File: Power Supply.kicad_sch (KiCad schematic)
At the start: 3 parts, among them J2 High Power Supply

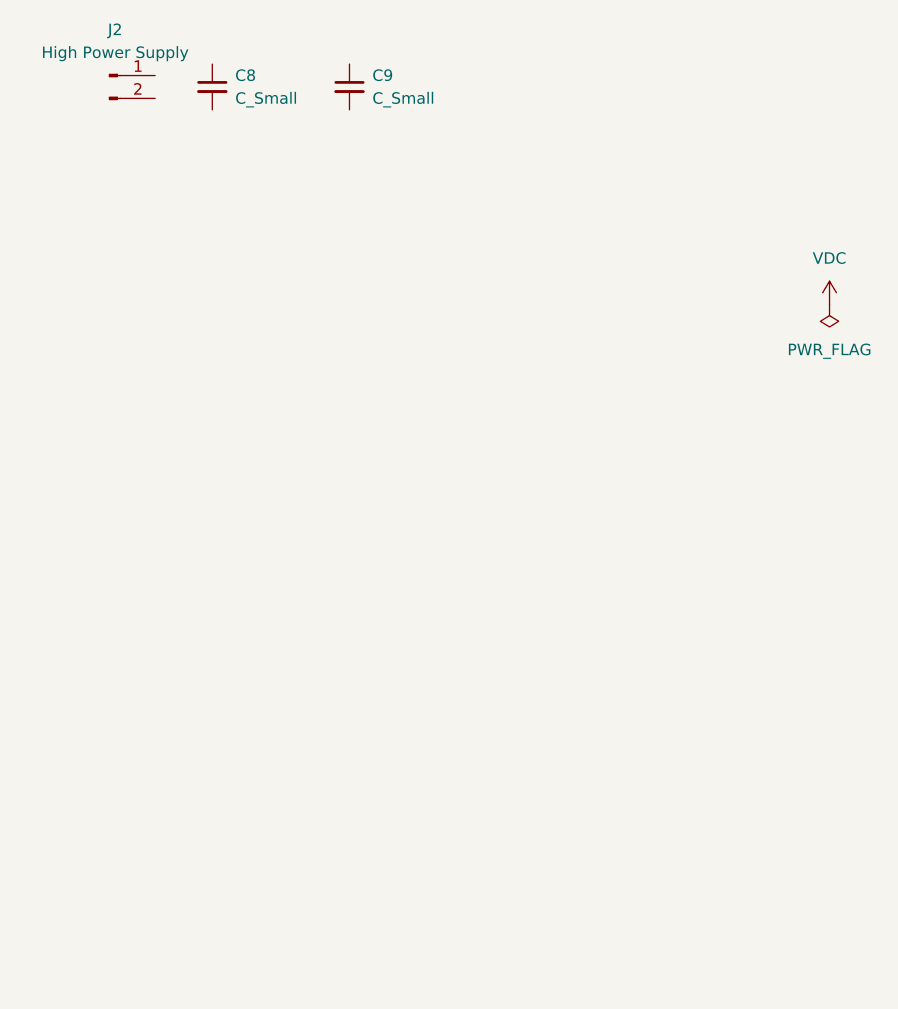
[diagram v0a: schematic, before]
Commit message: Pullup/pulldowns Footprints
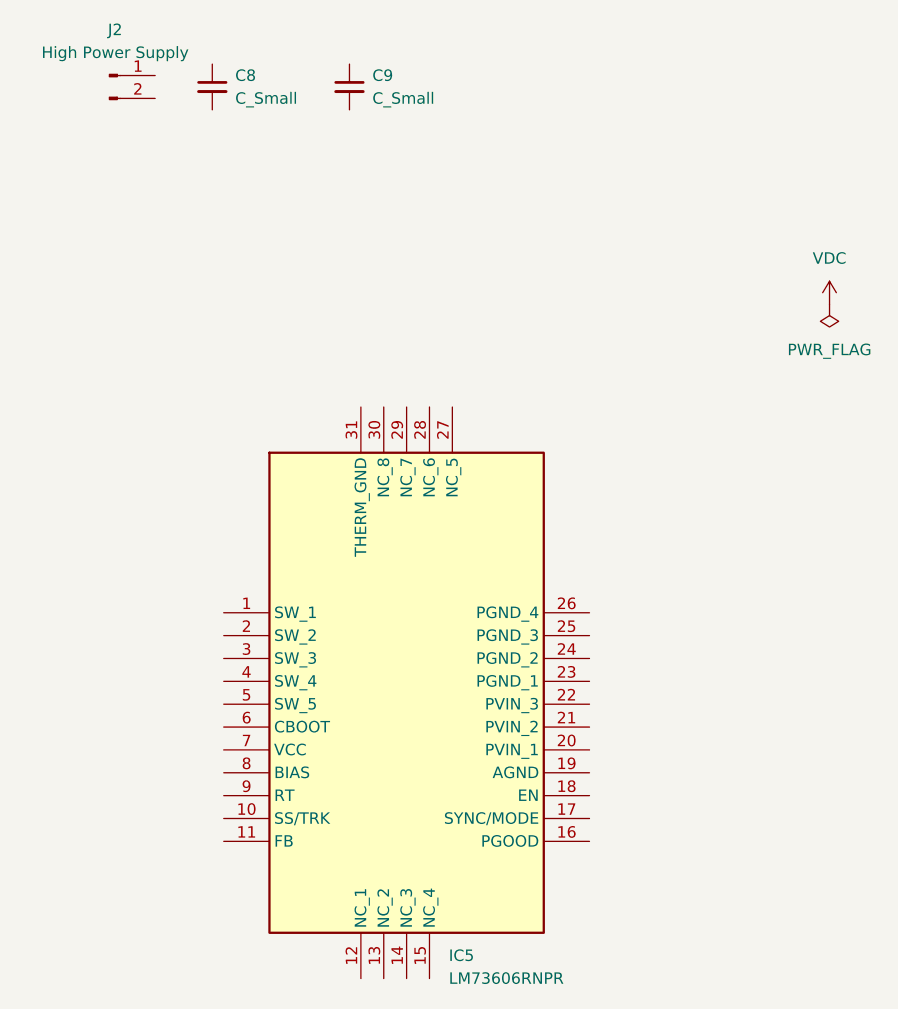
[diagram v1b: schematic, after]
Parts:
- added IC5: LM73606RNPR, Package_DFN_QFN:Texas_RNP0030B_WQFN-30-1EP_4x6mm_P0.5mm_EP1.8x4.5mm, symbol LM73606RNPR:LM73606RNPR
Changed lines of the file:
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@@
+	)
+	(symbol
+		(lib_id "LM73606RNPR:LM73606RNPR")
+		(at 41.91 90.17 0)
+		(unit 1)
+		(exclude_from_sim no)
+		(in_bom yes)
+		(on_board yes)
+		(dnp no)
+		(fields_autoplaced yes)
+		(property "Reference" "IC5"
+			(at 66.9133 128.27 0)
+			(effects
+				(font
+					(size 1.27 1.27)
+				)
+				(justify left)
+			)
+		)
+		(property "Value" "LM73606RNPR"
+			(at 66.9133 130.81 0)
+			(effects
+				(font
+					(size 1.27 1.27)
+				)
+				(justify left)
+			)
+		)
+		(property "Footprint" "Package_DFN_QFN:Texas_RNP0030B_WQFN-30-1EP_4x6mm_P0.5mm_EP1.8x4.5mm"
+			(at 78.74 169.85 0)
+			(effects
+				(font
+					(size 1.27 1.27)
+				)
+				(justify left top)
+				(hide yes)
+			)
+		)
+		(property "Datasheet" "http://www.ti.com/lit/ds/symlink/lm73606.pdf"
+			(at 78.74 269.85 0)
+			(effects
+				(font
+					(size 1.27 1.27)
+				)
+				(justify left top)
+				(hide yes)
+			)
+		)
+		(property "Description" "Switching Voltage Regulators 3.5V to 36V,6A Synch Step-Down Volt"
+			(at 41.91 90.17 0)
+			(effects
+				(font
+					(size 1.27 1.27)
+				)
+				(hide yes)
+			)
+		)
+		(property "Height" ""
+			(at 78.74 469.85 0)
+			(effects
+				(font
+					(size 1.27 1.27)
+				)
+				(justify left top)
+				(hide yes)
+			)
+		)
+		(property "Mouser Part Number" "595-LM73606RNPR"
+			(at 78.74 569.85 0)
+			(effects
+				(font
+					(size 1.27 1.27)
+				)
+				(justify left top)
+				(hide yes)
+			)
+		)
+		(property "Mouser Price/Stock" "https://www.mouser.co.uk/ProductDetail/Texas-Instruments/LM73606RNPR?qs=1mbolxNpo8cvH90iE325zw%3D%3D"
+			(at 78.74 669.85 0)
+			(effects
+				(font
+					(size 1.27 1.27)
+				)
+				(justify left top)
+				(hide yes)
+			)
+		)
+		(property "Manufacturer_Name" "Texas Instruments"
+			(at 78.74 769.85 0)
+			(effects
+				(font
+					(size 1.27 1.27)
+				)
+				(justify left top)
+				(hide yes)
+			)
+		)
+		(property "Manufacturer_Part_Number" "LM73606RNPR"
+			(at 78.74 869.85 0)
+			(effects
+				(font
+					(size 1.27 1.27)
+				)
+				(justify left top)
+				(hide yes)
+			)
+		)
+		(pin "5"
+		)
+		(pin "6"
+		)
+		(pin "9"
+		)
+		(pin "27"
+		)
+		(pin "8"
+		)
+		(pin "1"
+		)
+		(pin "2"
+		)
+		(pin "7"
+		)
+		(pin "3"
+		)
+		(pin "4"
+		)
+		(pin "11"
+		)
+		(pin "31"
+		)
+		(pin "12"
+		)
+		(pin "30"
+		)
+		(pin "10"
+		)
+		(pin "13"
+		)
+		(pin "29"
+		)
+		(pin "14"
+		)
+		(pin "28"
+		)
+		(pin "15"
+		)
+		(pin "26"
+		)
+		(pin "25"
+		)
+		(pin "21"
+		)
+		(pin "20"
+		)
+		(pin "24"
+		)
+		(pin "23"
+		)
+		(pin "22"
+		)
+		(pin "19"
+		)
+		(pin "18"
+		)
+		(pin "17"
+		)
+		(pin "16"
+		)
+		(instances
+			(project ""
+				(path "/ae336cd7-2593-4218-978e-a7691697d69e/64d25e49-7e7d-43ef-b4a7-b777bdf7e4a9"
+					(reference "IC5")
+					(unit 1)
+				)
+			)
+		)
 	)
 	(symbol

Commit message: Fin drivers, start voltage reg
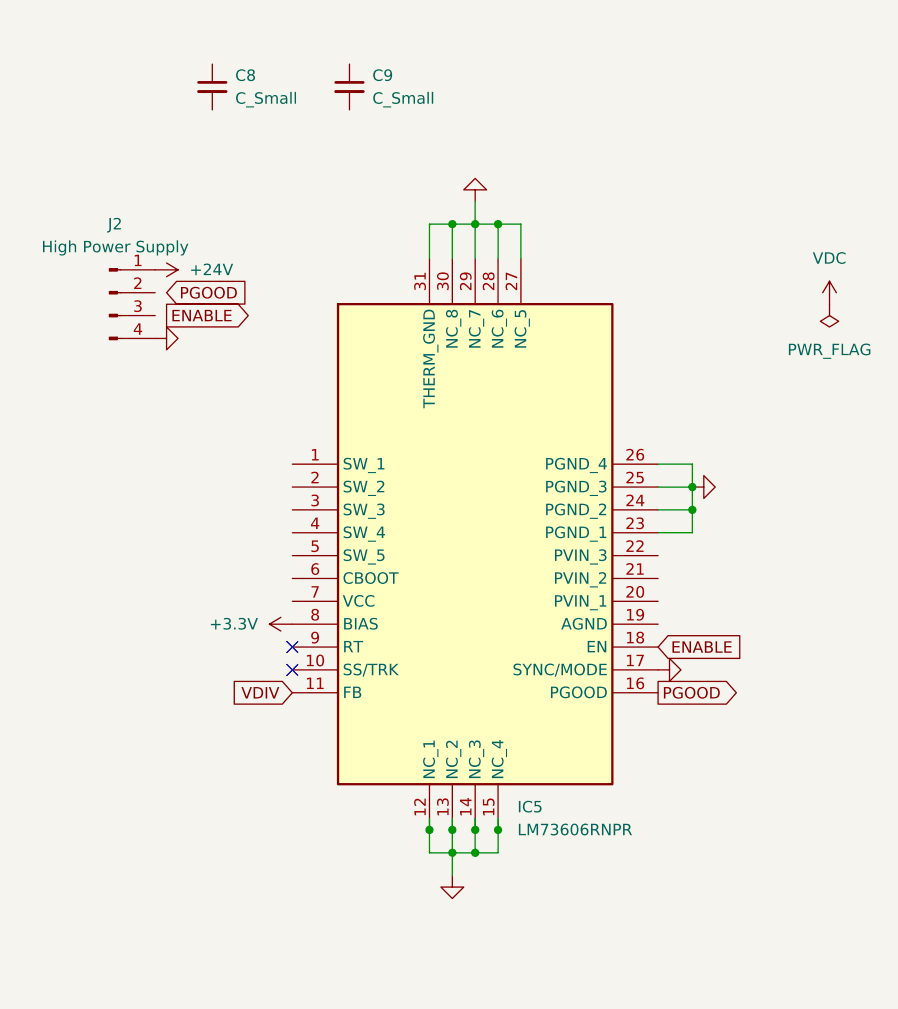
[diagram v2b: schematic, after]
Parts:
- J2: footprint (none) -> Connector_PinHeader_2.54mm:PinHeader_1x02_P2.54mm_Vertical; symbol Connector:Conn_01x02_Pin -> Connector:Conn_01x04_Pin
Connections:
- net VDIV: now reaches IC5.11 (FB)
- net GND: now reaches IC5.12 (NC_1)
- net GND: now also IC5.13 (NC_2), IC5.14 (NC_3), IC5.15 (NC_4), IC5.17 (SYNC/MODE), IC5.23 (PGND_1), IC5.24 (PGND_2), IC5.25 (PGND_3), IC5.26 (PGND_4), IC5.27 (NC_5), IC5.28 (NC_6), IC5.29 (NC_7), IC5.30 (NC_8), IC5.31 (THERM_GND), J2.4 (Pin_4)
- net PGOOD: now reaches IC5.16 (PGOOD)
- net ENABLE: now reaches IC5.18 (EN)
- net +3.3V: now reaches IC5.8 (BIAS)
- net +24V: now reaches J2.1 (Pin_1)
- no-connect marks 0 -> 2
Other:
- moved on the sheet: IC5
